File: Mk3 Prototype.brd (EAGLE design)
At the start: 113 x 53.5 mm, 132 parts, among them IC1 STM32F401R, IC2 CC3100, IC3 S25FL216K0PMFI011, J1 ZX62-AB-5PA(11), J2 SWD_SHROUD_SMD, J4 Arduino Headers, J7 SFV30R-2STE1HLF, Q1 BSS84W, Q10 2N7002KW, Q11 BSS84W, Q12 2N7002KW, U1 USD-SOCKETNEW, U2 JHD12864-G13BSW-OUTLINE, U3 MCP73831, X1 ABS07-32.768KHZ-T, X2 Q24FA20H00396, X3 CRYSTAL-3.2-2.5, X4 ABS07-32.768KHZ-T, Y1 AH316M245001-T

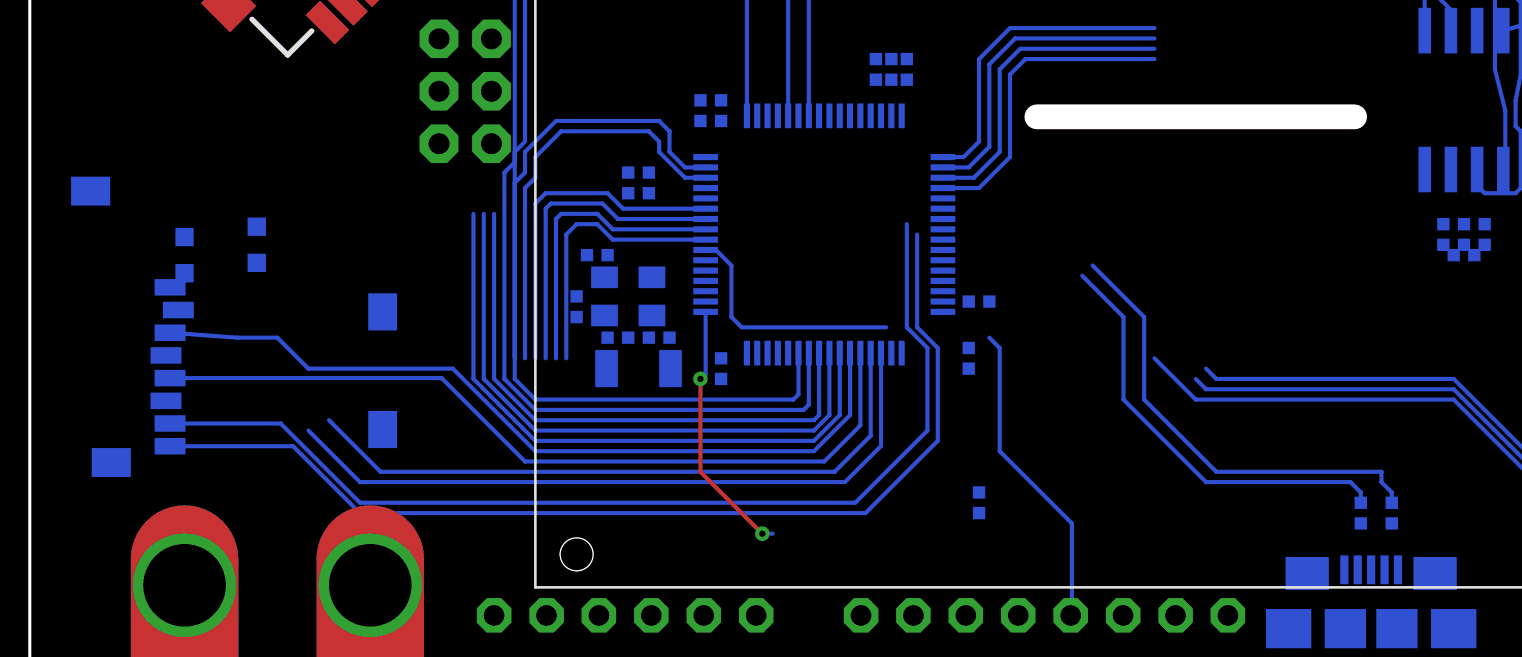
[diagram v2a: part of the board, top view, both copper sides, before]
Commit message: added gnd loop
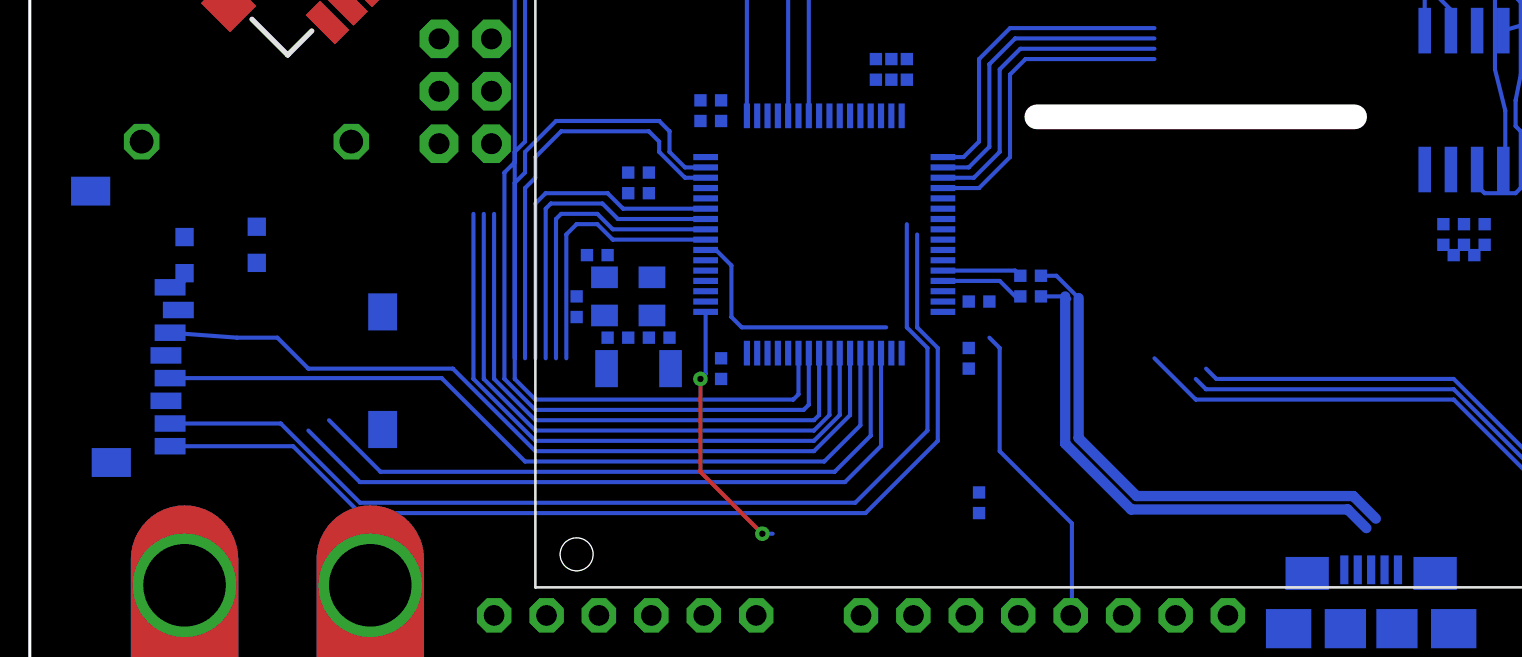
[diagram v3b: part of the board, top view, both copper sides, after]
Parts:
- added G1: GND-LOOPL, dtb:GND-LOOP-0.4
- moved R15 20.9 mm to (48.5, 19.0), turned to 180 degrees
- moved R16 19.1 mm to (48.5, 18.0), turned to 180 degrees
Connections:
- net GND: now also G1.P$3, G1.P$4
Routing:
- net USB_D_N: track 0.00 -> 25.1 mm
- net USB_D_P: track 0.00 -> 24.8 mm
- net D_N: track 22.2 -> 3.85 mm
- net D_P: track 20.7 -> 3.99 mm
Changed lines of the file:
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@@
 <?xml version="1.0" encoding="utf-8"?>
 <!DOCTYPE eagle SYSTEM "eagle.dtd">
-<eagle version="6.6.0">
+<eagle version="6.5.0">
 <drawing>
 <settings>
@@
 <element name="C34" library="TiLDA Mk3 Parts" package="C0402-SMALLER" value="0402/1u/10V/X5R" x="90" y="11" rot="MR270"/>
 <element name="R14" library="TiLDA Mk3 Parts" package="R0402-SMALLER" value="0402/100K/5%" x="46" y="8" rot="MR270"/>
-<element name="R15" library="TiLDA Mk3 Parts" package="R0402-SMALLER" value="22" x="66" y="7.5" rot="MR270"/>
-<element name="R16" library="TiLDA Mk3 Parts" package="R0402-SMALLER" value="22" x="64.5" y="7.5" rot="MR270"/>
+<element name="R15" library="TiLDA Mk3 Parts" package="R0402-SMALLER" value="22" x="48.5" y="19" rot="MR180"/>
+<element name="R16" library="TiLDA Mk3 Parts" package="R0402-SMALLER" value="22" x="48.5" y="18" rot="MR180"/>
 <element name="X3" library="TiLDA Mk3 Parts" package="CRYSTAL-3.2-2.5" value="CRYSTAL-3.2-2.5" x="29" y="18" rot="MR180"/>
 <element name="C35" library="TiLDA Mk3 Parts" package="C0402-SMALLER" value="0402/12p/50V/NP0" x="26.5" y="17.5" rot="MR90"/>
@@
 <element name="L5" library="TiLDA Mk3 Parts" package="WUERTH-0805" value="Bead" x="-35" y="-34.5"/>
 <element name="JP3" library="TiLDA Mk3 Parts" package="PINHEAD_2X05_127" value="" x="78.5" y="-3" rot="R90"/>
+<element name="G1" library="dtb" package="GND-LOOP-0.4" value="GND-LOOPL" x="10.5" y="25.5" rot="MR0"/>
 </elements>
 <signals>
@@
 <contactref element="C32" pad="1"/>
 <contactref element="IC1" pad="12"/>
+<contactref element="G1" pad="P$3"/>
+<contactref element="G1" pad="P$4"/>
 <wire x1="82" y1="49.5" x2="82.2" y2="51" width="0" layer="19" extent="16-16"/>
 <wire x1="81" y1="49.5" x2="82" y2="49.5" width="0" layer="19" extent="16-16"/>
@@
 <wire x1="91.375" y1="30.125" x2="91.5" y2="34" width="0" layer="19" extent="1-16"/>
 <wire x1="85.5" y1="32.5" x2="89.875" y2="34" width="0" layer="19" extent="16-16"/>
-<wire x1="84.5" y1="31.5" x2="85.5" y2="31.5" width="0" layer="19" extent="1-1"/>
+<wire x1="84.5" y1="32.5" x2="85.5" y2="32.5" width="0" layer="19" extent="16-16"/>
 <wire x1="83" y1="31.5" x2="84" y2="32" width="0" layer="19" extent="16-16"/>
 <wire x1="80" y1="30.5" x2="83" y2="31.5" width="0" layer="19" extent="16-16"/>
@@
 <wire x1="30.15" y1="18.925" x2="27.85" y2="17.075" width="0" layer="19" extent="16-16"/>
 <wire x1="19.833" y1="25.4" x2="27" y2="20" width="0" layer="19" extent="16-16"/>
-<wire x1="11" y1="21.375" x2="19.833" y2="25.4" width="0" layer="19" extent="16-16"/>
+<wire x1="15.58" y1="25.5" x2="19.833" y2="25.4" width="0" layer="19" extent="1-1"/>
+<wire x1="11" y1="21.375" x2="15.58" y2="25.5" width="0" layer="19" extent="16-16"/>
 <wire x1="7.5" y1="20.875" x2="11" y2="21.375" width="0" layer="19" extent="16-16"/>
 <wire x1="2.95" y1="23.1" x2="7.5" y2="20.875" width="0" layer="19" extent="16-16"/>
+<wire x1="5.42" y1="25.5" x2="2.95" y2="23.1" width="0" layer="19" extent="16-16"/>
 <wire x1="6.6" y1="12.94" x2="7.5" y2="20.875" width="0" layer="19" extent="16-16"/>
 <wire x1="3.95" y1="9.95" x2="6.6" y2="12.94" width="0" layer="19" extent="16-16"/>
@@
 <wire x1="39" y1="9.5" x2="17" y2="9.5" width="0.2" layer="16"/>
 <wire x1="17" y1="9.5" x2="14.5" y2="12" width="0.2" layer="16"/>
-<wire x1="14.5" y1="12" x2="7.2" y2="17.34" width="0" layer="19" extent="16-16"/>
+<wire x1="7.2" y1="17.34" x2="14.5" y2="12" width="0" layer="19" extent="16-16"/>
 </signal>
 <signal name="SDIO_CMD">
@@
 <contactref element="IC1" pad="30"/>
 <contactref element="C10" pad="2"/>
-<wire x1="41" y1="29.5" x2="41.25" y2="26.75" width="0" layer="19" extent="16-16"/>
+<wire x1="41.25" y1="26.75" x2="41" y2="29.5" width="0" layer="19" extent="16-16"/>
 </signal>
 <signal name="N$13">
@@
 <contactref element="R15" pad="2"/>
 <contactref element="J1" pad="D-"/>
-<wire x1="65.65" y1="4.75" x2="66" y2="7" width="0" layer="19" extent="16-16"/>
+<wire x1="49" y1="19" x2="49.7474875" y2="19" width="0.2" layer="16"/>
+<wire x1="49.7474875" y1="19" x2="50.825" y2="17.9224875" width="0.2" layer="16"/>
+<wire x1="50.825" y1="17.9224875" x2="50.825" y2="11.134625" width="0.5" layer="16"/>
+<wire x1="50.825" y1="11.134625" x2="53.634625" y2="8.325" width="0.5" layer="16"/>
+<wire x1="53.634625" y1="8.325" x2="64.134625" y2="8.325" width="0.5" layer="16"/>
+<wire x1="64.134625" y1="8.325" x2="65.2298125" y2="7.2298125" width="0.5" layer="16"/>
+<wire x1="65.2298125" y1="7.2298125" x2="65.65" y2="4.75" width="0" layer="19" extent="1-16"/>
 </signal>
 <signal name="USB_D_P" class="2">
 <contactref element="R16" pad="2"/>
 <contactref element="J1" pad="D+"/>
-<wire x1="65" y1="4.75" x2="64.5" y2="7" width="0" layer="19" extent="16-16"/>
+<wire x1="49" y1="18" x2="50.175" y2="18" width="0.2" layer="16"/>
+<wire x1="50.2525125" y1="18" x2="50.37625625" y2="17.87625625" width="0.2" layer="16"/>
+<wire x1="50.175" y1="18" x2="50.175" y2="10.865375" width="0.5" layer="16"/>
+<wire x1="50.175" y1="10.865375" x2="53.365375" y2="7.675" width="0.5" layer="16"/>
+<wire x1="53.365375" y1="7.675" x2="63.865375" y2="7.675" width="0.5" layer="16"/>
+<wire x1="63.865375" y1="7.675" x2="64.7701875" y2="6.7701875" width="0.5" layer="16"/>
+<wire x1="64.7701875" y1="6.7701875" x2="65" y2="4.75" width="0" layer="19" extent="1-16"/>
 </signal>
 <signal name="D_N" class="2">
 <contactref element="R15" pad="1"/>
 <contactref element="IC1" pad="44"/>
-<wire x1="66" y1="8" x2="66" y2="8.5" width="0.2" layer="16"/>
-<wire x1="66" y1="8.5" x2="65.5" y2="9" width="0.2" layer="16"/>
-<wire x1="65.5" y1="9" x2="65.5" y2="9.5" width="0.2" layer="16"/>
-<wire x1="65.5" y1="9.5" x2="57.5" y2="9.5" width="0.2" layer="16"/>
-<wire x1="57.5" y1="9.5" x2="54" y2="13" width="0.2" layer="16"/>
-<wire x1="54" y1="13" x2="54" y2="17" width="0.2" layer="16"/>
-<wire x1="54" y1="17" x2="51.5" y2="19.5" width="0.2" layer="16"/>
-<wire x1="44.25" y1="19.25" x2="51.5" y2="19.5" width="0" layer="19" extent="16-16"/>
+<wire x1="44.25" y1="19.25" x2="47.75" y2="19.25" width="0.2" layer="16"/>
+<wire x1="47.75" y1="19.25" x2="48" y2="19" width="0.2" layer="16"/>
 </signal>
 <signal name="D_P" class="2">
 <contactref element="R16" pad="1"/>
 <contactref element="IC1" pad="45"/>
-<wire x1="64.5" y1="8" x2="64.5" y2="8.5" width="0.2" layer="16"/>
-<wire x1="64.5" y1="8.5" x2="64" y2="9" width="0.2" layer="16"/>
-<wire x1="64" y1="9" x2="57" y2="9" width="0.2" layer="16"/>
-<wire x1="57" y1="9" x2="53" y2="13" width="0.2" layer="16"/>
-<wire x1="53" y1="13" x2="53" y2="17" width="0.2" layer="16"/>
-<wire x1="53" y1="17" x2="51" y2="19" width="0.2" layer="16"/>
-<wire x1="44.25" y1="18.75" x2="51" y2="19" width="0" layer="19" extent="16-16"/>
+<wire x1="44.25" y1="18.75" x2="47.0025125" y2="18.75" width="0.2" layer="16"/>
+<wire x1="47.0025125" y1="18.75" x2="47.87625625" y2="17.87625625" width="0.2" layer="16"/>
 </signal>
 <signal name="N$31">
@@
 <contactref element="Q1" pad="2"/>
 <contactref element="S5" pad="2"/>
-<wire x1="-20.35" y1="-22.425" x2="-21.7" y2="-28.5" width="0" layer="19" extent="1-1"/>
-<wire x1="108.75" y1="18.25" x2="-20.35" y2="-22.425" width="0" layer="19" extent="1-16"/>
+<wire x1="-20.35" y1="-22.425" x2="108.75" y2="18.25" width="0" layer="19" extent="1-16"/>
+<wire x1="-21.7" y1="-28.5" x2="-20.35" y2="-22.425" width="0" layer="19" extent="1-1"/>
 </signal>
 <signal name="N$41">
@@
 <wire x1="21" y1="45.5" x2="20.5" y2="45" width="0.2" layer="1"/>
 <wire x1="-33" y1="-31" x2="-37" y2="-31" width="0" layer="19" extent="1-1"/>
-<wire x1="34.75" y1="26.75" x2="-33" y2="-31" width="0" layer="19" extent="1-16"/>
-<wire x1="13.75" y1="44.5" x2="20.5" y2="45" width="0" layer="19" extent="1-1"/>
+<wire x1="13.75" y1="44.5" x2="-33" y2="-31" width="0" layer="19" extent="1-1"/>
+<wire x1="20.5" y1="45" x2="13.75" y2="44.5" width="0" layer="19" extent="1-1"/>
 </signal>
 <signal name="SPI1_CLK">
